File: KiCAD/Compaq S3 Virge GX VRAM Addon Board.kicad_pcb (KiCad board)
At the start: 4 copper layers, 70 x 70 mm, 22 parts, among them U3 SST39SF010-040

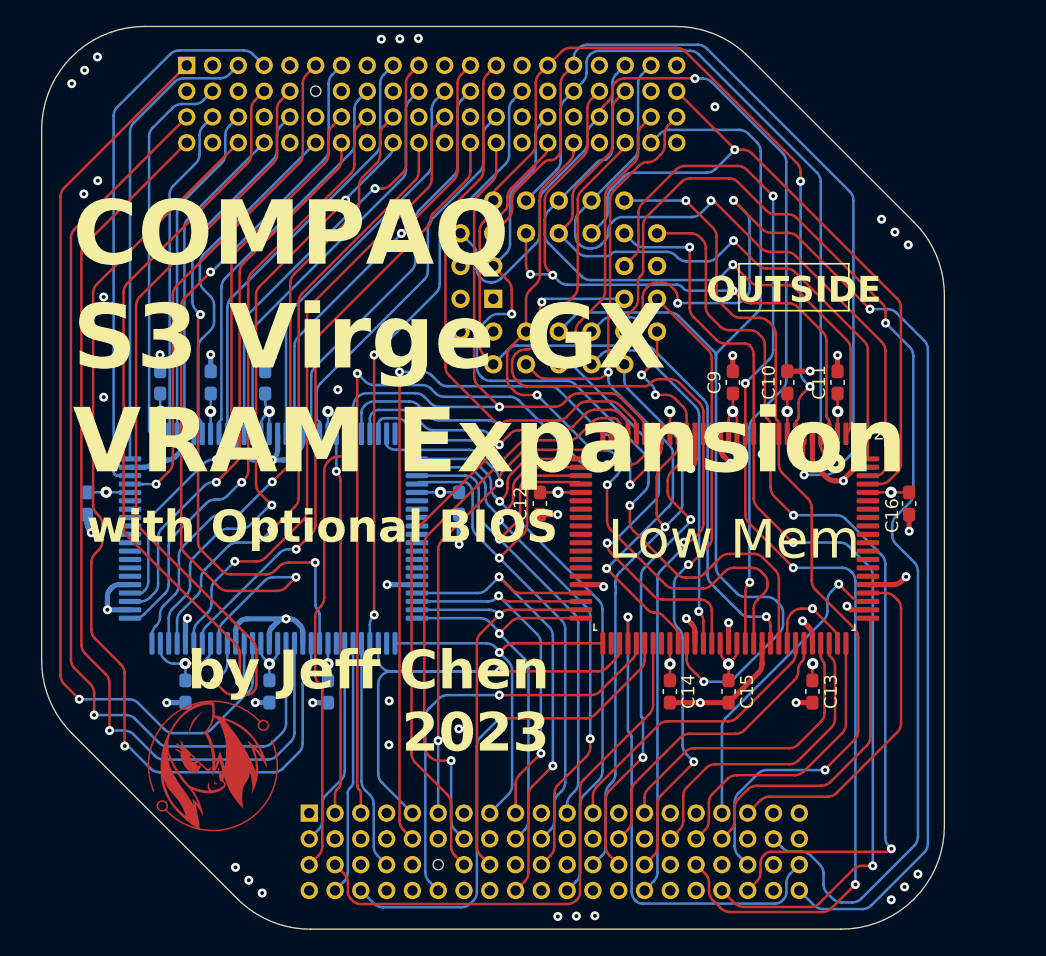
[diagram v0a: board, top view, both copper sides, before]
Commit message: Update PCB project
Add Mystique 220 compatibility
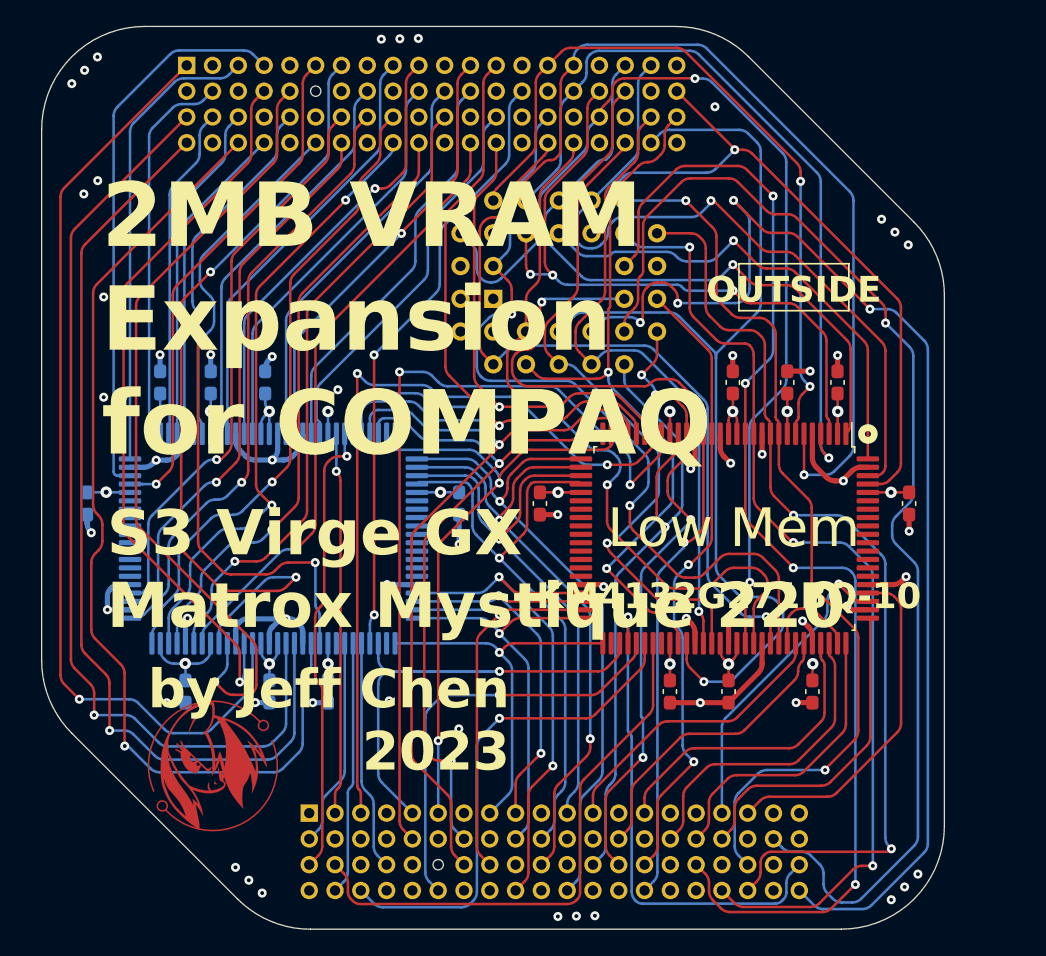
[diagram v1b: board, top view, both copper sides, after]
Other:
- board text added: "2MB VRAM Expansion for COMPAQ"
- board text added: "Optional S3 BIOS"
- board text added: "S3 Virge GX Matrox Mystique 220"
- board text removed: "COMPAQ S3 Virge GX VRAM Expansion"
- board text removed: "Optional BIOS"
- board text removed: "with Optional BIOS"
